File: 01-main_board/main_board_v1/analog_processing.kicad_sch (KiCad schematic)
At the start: 21 parts, among them IC6 AD7175-8BCPZ-RL7

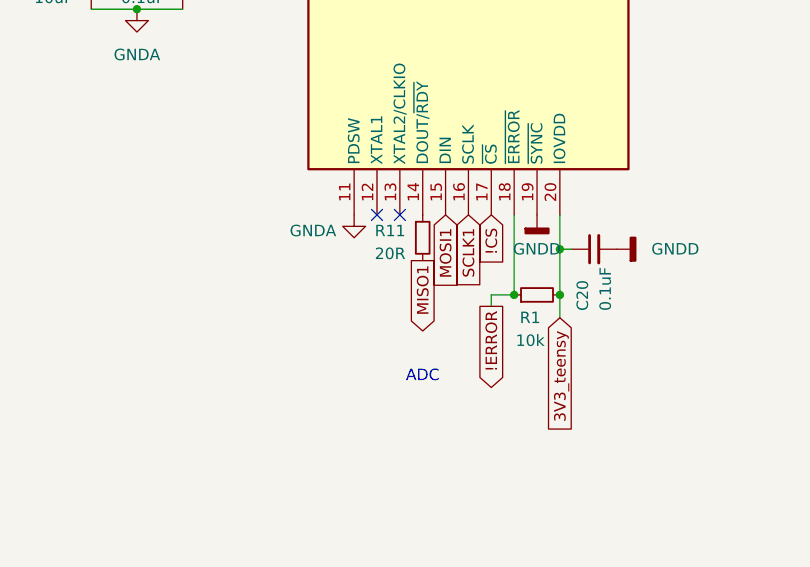
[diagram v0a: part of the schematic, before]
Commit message: fixed/set all resistors to standard values
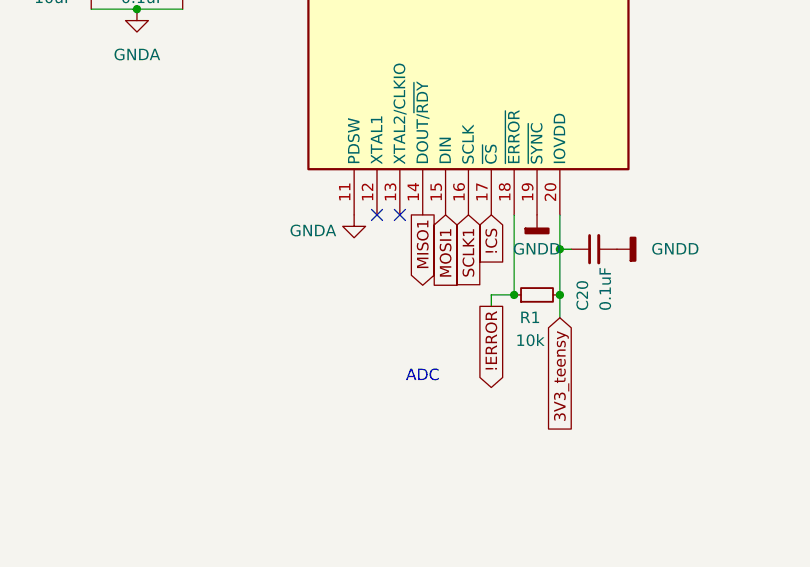
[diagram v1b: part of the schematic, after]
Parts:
- removed R11: 20R, symbol Device:R_Small
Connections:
- net MISO1: now also IC6.14 (DOUT/~{RDY})
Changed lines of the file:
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@@
 	(global_label "MISO1"
 		(shape output)
-		(at 74.93 128.27 270)
+		(at 74.93 123.19 270)
 		(fields_autoplaced yes)
 		(effects
@@
 		)
 		(property "Intersheetrefs" "${INTERSHEET_REFS}"
-			(at 74.93 137.0609 90)
+			(at 74.93 131.9809 90)
 			(effects
 				(font
@@
 					(unit 1)
 				)
-			)
-		)
-	)
-	(symbol
-		(lib_id "Device:R_Small")
-		(at 74.93 125.73 0)
-		(unit 1)
-		(exclude_from_sim no)
-		(in_bom yes)
-		(on_board yes)
-		(dnp no)
-		(property "Reference" "R11"
-			(at 69.596 124.968 0)
-			(effects
-				(font
-					(size 1.27 1.27)
-				)
-				(justify left)
-			)
-		)
-		(property "Value" "20R"
-			(at 69.596 127.508 0)
-			(effects
-				(font
-					(size 1.27 1.27)
-				)
-				(justify left)
-			)
-		)
-		(property "Footprint" ""
-			(at 74.93 125.73 0)
-			(effects
-				(font
-					(size 1.27 1.27)
-				)
-				(hide yes)
-			)
-		)
-		(property "Datasheet" "~"
-			(at 74.93 125.73 0)
-			(effects
-				(font
-					(size 1.27 1.27)
-				)
-				(hide yes)
-			)
-		)
-		(property "Description" "Resistor, small symbol"
-			(at 74.93 125.73 0)
-			(effects
-				(font
-					(size 1.27 1.27)
-				)
-				(hide yes)
-			)
-		)
-		(pin "2"
-		)
-		(pin "1"
-		)
-		(instances
-			(project "main_board_v1"
-				(path "/12c2237c-5932-49af-9119-92b28c846ae7/3932ebef-992a-45fd-a214-7d9aa3b763ff"
-					(reference "R11")
-					(unit 1)
-				)

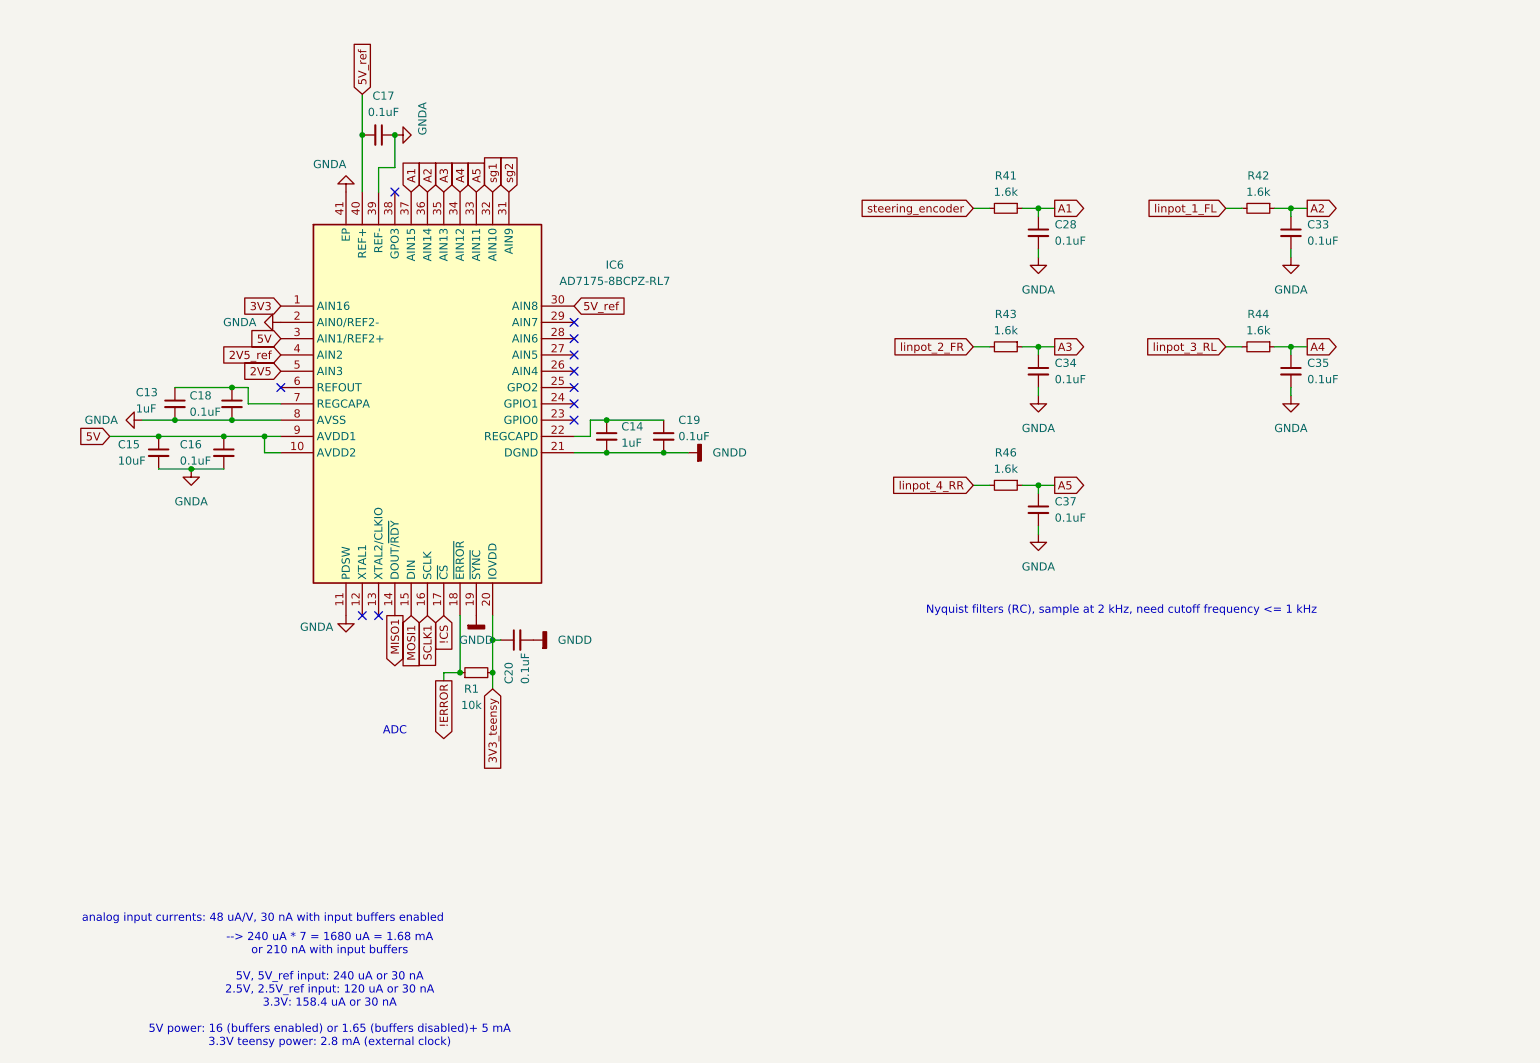
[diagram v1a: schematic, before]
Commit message: addressed misc changes on review notes gdoc
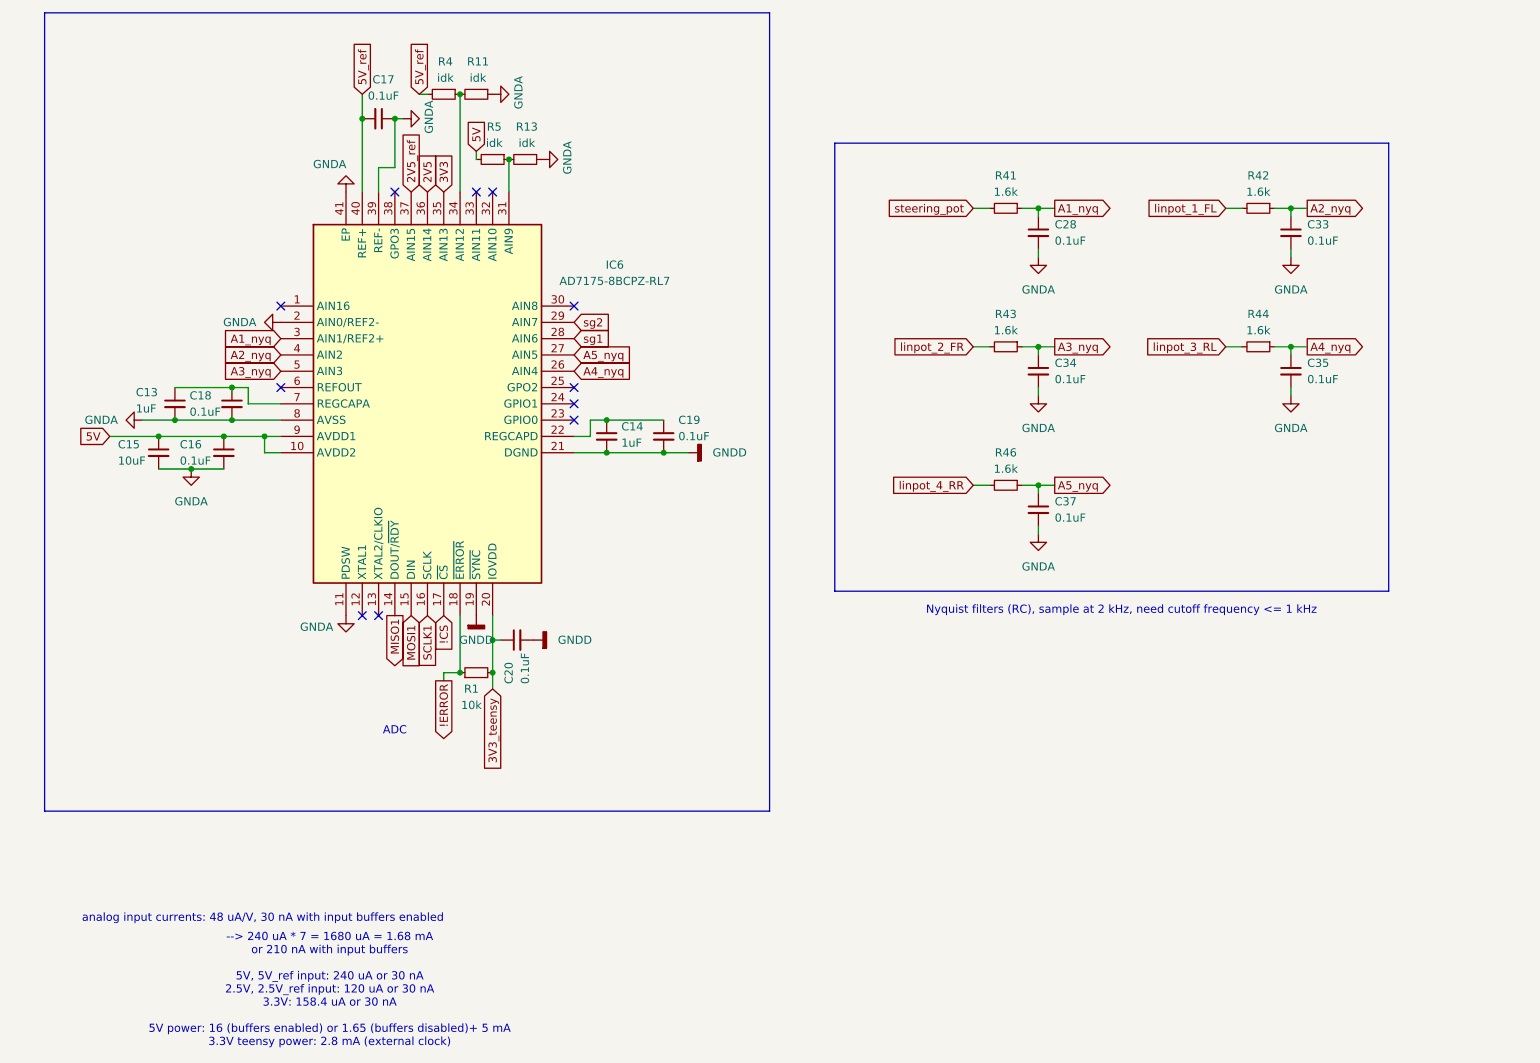
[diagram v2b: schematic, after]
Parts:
- added R11, R13, R4, R5: idk, symbol Device:R_Small
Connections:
- net 2V5: now also IC6.36 (AIN14); no longer IC6.5 (AIN3)
- net 2V5_ref: now also IC6.37 (AIN15); no longer IC6.4 (AIN2)
- net 3V3: now also IC6.35 (AIN13); no longer IC6.1 (AIN16)
- net 5V: now also R5.2; no longer IC6.3 (AIN1/REF2+)
- net 5V_ref: now also R4.2; no longer IC6.30 (AIN8)
- net GNDA: now also R11.1, R13.1
- net sg1: now also IC6.28 (AIN6); no longer IC6.32 (AIN10)
- net sg2: now also IC6.29 (AIN7); no longer IC6.31 (AIN9)
- net A4_nyq: now reaches IC6.26 (AIN4)
- net A4_nyq: now also C35.1, R44.1
- net A5_nyq: now reaches IC6.27 (AIN5)
- net A5_nyq: now also C37.1, R46.1
- net A1 renamed A1_nyq
- net A1_nyq: now also IC6.3 (AIN1/REF2+); no longer IC6.37 (AIN15)
- net A2 renamed A2_nyq
- net A2_nyq: now also IC6.4 (AIN2); no longer IC6.36 (AIN14)
- net A3 renamed A3_nyq
- net A3_nyq: now also IC6.5 (AIN3); no longer IC6.35 (AIN13)
- removed net A4: C35.1, IC6.34 (AIN12), R44.1
- removed net A5: C37.1, IC6.33 (AIN11), R46.1
- net steering_encoder renamed steering_pot
- new net: IC6.34 (AIN12), R11.2, R4.1
- new net: IC6.31 (AIN9), R13.2, R5.1
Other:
- moved on the sheet: C17

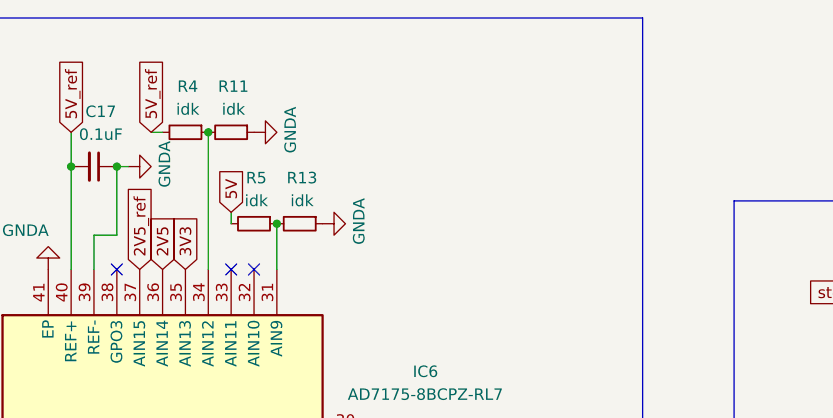
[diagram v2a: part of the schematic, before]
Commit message: added/changed footprints to 402s and solderable packages
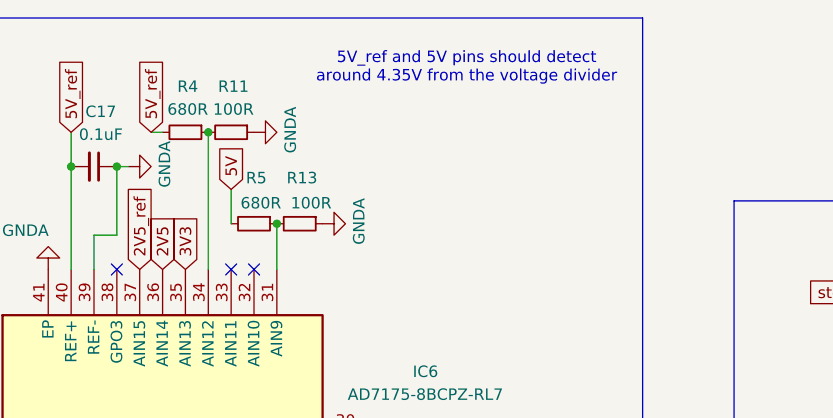
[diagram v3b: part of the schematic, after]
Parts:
- C13, C14, C15, C16, C17, C18, C19, C20, C28, C33, C34, C35, C37: footprint (none) -> Capacitor_SMD:C_0402_1005Metric
- R1, R41, R42, R43, R44, R46: footprint (none) -> Resistor_SMD:R_0402_1005Metric
- R11, R13: value idk -> 100R; footprint (none) -> Resistor_SMD:R_0402_1005Metric
- R4, R5: value idk -> 680R; footprint (none) -> Resistor_SMD:R_0402_1005Metric
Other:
- note added: "5V_ref and 5V pins should detect around 4.35V from the voltage divider"
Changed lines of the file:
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@@
 		)
 	)
+	(text "5V_ref and 5V pins should detect\naround 4.35V from the voltage divider\n"
+		(exclude_from_sim no)
+		(at 113.792 33.02 0)
+		(effects
+			(font
+				(size 1.27 1.27)
+			)
+			(justify top)
+		)
+	)
 	(junction
 		(at 107.95 92.71)
@@
 	(wire
 		(pts
-			(xy 87.63 50.8) (xy 87.63 52.07)
+			(xy 87.63 48.26) (xy 87.63 52.07)
 		)
 		(stroke
@@
 	(global_label "5V"
 		(shape input)
-		(at 87.63 50.8 90)
+		(at 87.63 48.26 90)
 		(fields_autoplaced yes)
 		(effects
@@
 		)
 		(property "Intersheetrefs" "${INTERSHEET_REFS}"
-			(at 87.63 45.5167 90)
+			(at 87.63 42.9767 90)
 			(effects
 				(font
@@
 			)
 		)
-		(property "Value" "idk"
+		(property "Value" "100R"
 			(at 87.884 39.37 90)
 			(effects
@@
 			)
 		)
-		(property "Footprint" ""
+		(property "Footprint" "Resistor_SMD:R_0402_1005Metric"
 			(at 87.63 41.91 0)
 			(effects
@@
 			)
 		)
-		(property "Footprint" ""
+		(property "Footprint" "Capacitor_SMD:C_0402_1005Metric"
 			(at 72.39 45.72 0)
 			(effects
@@
 			)
 		)
-		(property "Value" "idk"
+		(property "Value" "680R"
 			(at 82.804 39.37 90)
 			(effects
@@
 			)
 		)
-		(property "Footprint" ""
+		(property "Footprint" "Resistor_SMD:R_0402_1005Metric"
 			(at 82.55 41.91 0)
 			(effects
@@
 			)
 		)
-		(property "Footprint" ""
+		(property "Footprint" "Resistor_SMD:R_0402_1005Metric"
 			(at 170.18 81.28 0)
 			(effects
@@
 			)
 		)
-		(property "Footprint" ""
+		(property "Footprint" "Resistor_SMD:R_0402_1005Metric"
 			(at 170.18 59.69 0)
 			(effects
@@
 			)
 		)
-		(property "Footprint" ""
+		(property "Footprint" "Capacitor_SMD:C_0402_1005Metric"
 			(at 116.84 95.25 0)
 			(effects
@@
 			)
 		)
-		(property "Footprint" ""
+		(property "Footprint" "Resistor_SMD:R_0402_1005Metric"
 			(at 209.55 81.28 0)
 			(effects
@@
 			)
 		)
-		(property "Footprint" ""
+		(property "Footprint" "Resistor_SMD:R_0402_1005Metric"
 			(at 87.63 132.08 0)
 			(effects
@@
 			)
 		)
-		(property "Footprint" ""
+		(property "Footprint" "Capacitor_SMD:C_0402_1005Metric"
 			(at 49.53 90.17 0)
 			(effects
@@
 			)
 		)
-		(property "Footprint" ""
+		(property "Footprint" "Capacitor_SMD:C_0402_1005Metric"
 			(at 93.98 127 0)
 			(effects
@@
 			)
 		)
-		(property "Footprint" ""
+		(property "Footprint" "Capacitor_SMD:C_0402_1005Metric"
 			(at 40.64 90.17 0)
 			(effects
@@
 			)
 		)
-		(property "Footprint" ""
+		(property "Footprint" "Capacitor_SMD:C_0402_1005Metric"
 			(at 107.95 95.25 0)
 			(effects
@@
 			)
 		)
-		(property "Footprint" ""
+		(property "Footprint" "Capacitor_SMD:C_0402_1005Metric"
 			(at 214.63 63.5 0)
 			(effects
@@
 			)
 		)
-		(property "Footprint" ""
+		(property "Footprint" "Capacitor_SMD:C_0402_1005Metric"
 			(at 175.26 85.09 0)
 			(effects
@@
 			)
 		)
-		(property "Value" "idk"
-			(at 95.504 49.53 90)
+		(property "Value" "100R"
+			(at 96.52 49.784 90)
 			(effects
 				(font
@@
 			)
 		)
-		(property "Footprint" ""
+		(property "Footprint" "Resistor_SMD:R_0402_1005Metric"
 			(at 95.25 52.07 0)
 			(effects
@@
 			)
 		)
-		(property "Footprint" ""
+		(property "Footprint" "Resistor_SMD:R_0402_1005Metric"
 			(at 209.55 59.69 0)
 			(effects
@@
 			)
 		)
-		(property "Footprint" ""
+		(property "Footprint" "Capacitor_SMD:C_0402_1005Metric"
 			(at 48.26 97.79 0)
 			(effects
@@
 			)
 		)
-		(property "Footprint" ""
+		(property "Footprint" "Capacitor_SMD:C_0402_1005Metric"
 			(at 38.1 97.79 0)
 			(effects
@@
 			)
 		)
-		(property "Footprint" ""
+		(property "Footprint" "Resistor_SMD:R_0402_1005Metric"
 			(at 170.18 102.87 0)
 			(effects
@@
 			)
 		)
-		(property "Value" "idk"
-			(at 90.424 49.53 90)
+		(property "Value" "680R"
+			(at 90.932 49.784 90)
 			(effects
 				(font
@@
 			)
 		)
-		(property "Footprint" ""
+		(property "Footprint" "Resistor_SMD:R_0402_1005Metric"
 			(at 90.17 52.07 0)
 			(effects
@@
 			)
 		)
-		(property "Footprint" ""
+		(property "Footprint" "Capacitor_SMD:C_0402_1005Metric"
 			(at 175.26 63.5 0)
 			(effects
@@
 			)
 		)
-		(property "Footprint" ""
+		(property "Footprint" "Capacitor_SMD:C_0402_1005Metric"
 			(at 175.26 106.68 0)
 			(effects
@@
 			)
 		)
-		(property "Footprint" ""
+		(property "Footprint" "Capacitor_SMD:C_0402_1005Metric"
 			(at 214.63 85.09 0)
 			(effects

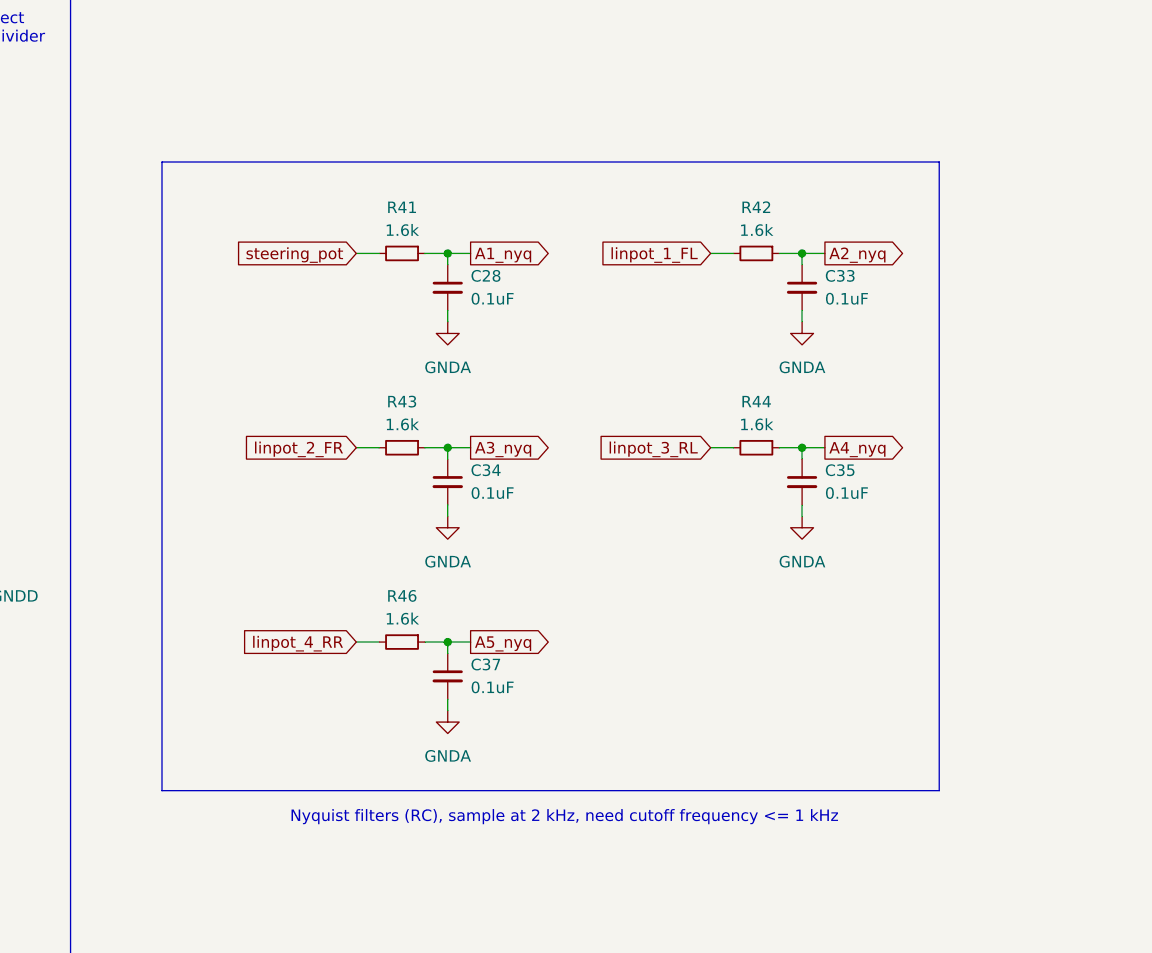
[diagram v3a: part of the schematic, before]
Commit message: added optional offset to the nyquist filters for testing later
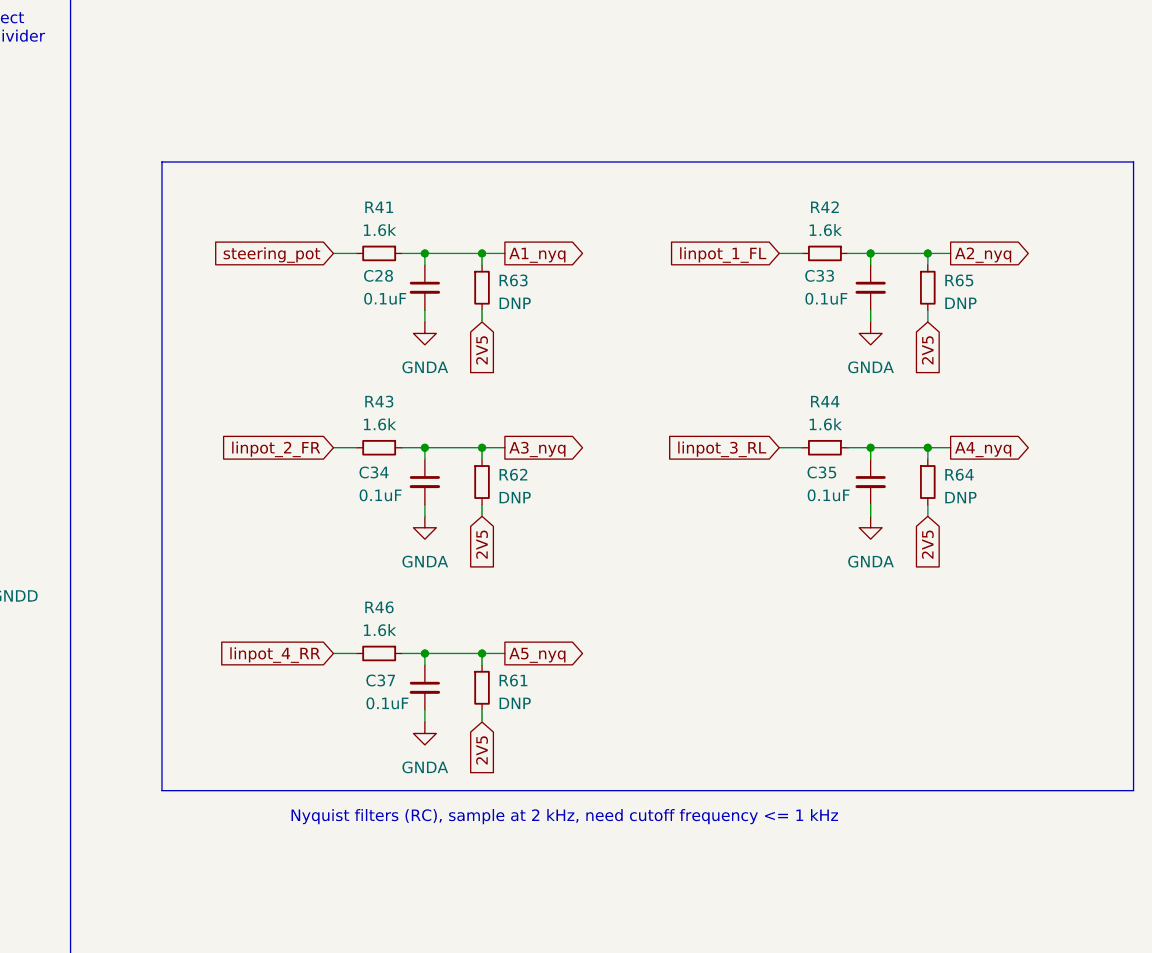
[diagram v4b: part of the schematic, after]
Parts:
- added R61, R62, R63, R64, R65: DNP, Resistor_SMD:R_0402_1005Metric, symbol Device:R_Small
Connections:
- net 2V5: now also R61.2, R62.2, R63.2, R64.2, R65.2
- net A1_nyq: now also R63.1
- net A2_nyq: now also R65.1
- net A3_nyq: now also R62.1
- net A4_nyq: now also R64.1
- net A5_nyq: now also R61.1
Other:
- moved on the sheet: C28, C33, C34, C35, C37, R41, R42, R43, R44, R46
